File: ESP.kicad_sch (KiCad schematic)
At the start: 23 parts, among them J9 USB_C_Receptacle_USB2.0_16P, U2 TLV1117LV33DCYR, U4 ESP32-C6-MINI-1/U

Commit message: replaced 0805 with 0603, changed logic analyzer symbol and silkscreen
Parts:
- C10, C11, C12, C13, C6, C7, C8, C9: footprint Capacitor_SMD:C_0805_2012Metric -> Capacitor_SMD:C_0603_1608Metric
- D2, D3: footprint LED_SMD:LED_0805_2012Metric -> LED_SMD:LED_0603_1608Metric
- R10, R11, R6, R7, R8, R9: footprint Resistor_SMD:R_0805_2012Metric -> Resistor_SMD:R_0603_1608Metric
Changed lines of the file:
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@@
 			)
 		)
-		(property "Footprint" "Resistor_SMD:R_0805_2012Metric"
+		(property "Footprint" "Resistor_SMD:R_0603_1608Metric"
 			(at 58.166 51.054 90)
 			(effects
@@
 			)
 		)
-		(property "Footprint" "Capacitor_SMD:C_0805_2012Metric"
+		(property "Footprint" "Capacitor_SMD:C_0603_1608Metric"
 			(at 55.5752 151.13 0)
 			(effects
@@
 			)
 		)
-		(property "Footprint" "Capacitor_SMD:C_0805_2012Metric"
+		(property "Footprint" "Capacitor_SMD:C_0603_1608Metric"
 			(at 107.6452 53.34 0)
 			(effects
@@
 			)
 		)
-		(property "Footprint" "Resistor_SMD:R_0805_2012Metric"
+		(property "Footprint" "Resistor_SMD:R_0603_1608Metric"
 			(at 25.146 141.224 90)
 			(effects
@@
 			)
 		)
-		(property "Footprint" "Resistor_SMD:R_0805_2012Metric"
+		(property "Footprint" "Resistor_SMD:R_0603_1608Metric"
 			(at 37.846 141.224 90)
 			(effects
@@
 			)
 		)
-		(property "Footprint" "Resistor_SMD:R_0805_2012Metric"
+		(property "Footprint" "Resistor_SMD:R_0603_1608Metric"
 			(at 94.996 34.544 90)
 			(effects
@@
 			)
 		)
-		(property "Footprint" "Capacitor_SMD:C_0805_2012Metric"
+		(property "Footprint" "Capacitor_SMD:C_0603_1608Metric"
 			(at 49.2252 53.34 0)
 			(effects
@@
 			)
 		)
-		(property "Footprint" "LED_SMD:LED_0805_2012Metric"
+		(property "Footprint" "LED_SMD:LED_0603_1608Metric"
 			(at 36.83 151.13 0)
 			(effects
@@
 			)
 		)
-		(property "Footprint" "Capacitor_SMD:C_0805_2012Metric"
+		(property "Footprint" "Capacitor_SMD:C_0603_1608Metric"
 			(at 35.2552 46.99 0)
 			(effects
@@
 			)
 		)
-		(property "Footprint" "LED_SMD:LED_0805_2012Metric"
+		(property "Footprint" "LED_SMD:LED_0603_1608Metric"
 			(at 24.13 151.13 0)
 			(effects
@@
 			)
 		)
-		(property "Footprint" "Resistor_SMD:R_0805_2012Metric"
+		(property "Footprint" "Resistor_SMD:R_0603_1608Metric"
 			(at 232.791 144.399 90)
 			(effects
@@
 			)
 		)
-		(property "Footprint" "Capacitor_SMD:C_0805_2012Metric"
+		(property "Footprint" "Capacitor_SMD:C_0603_1608Metric"
 			(at 70.8152 92.71 0)
 			(effects
@@
 			)
 		)
-		(property "Footprint" "Capacitor_SMD:C_0805_2012Metric"
+		(property "Footprint" "Capacitor_SMD:C_0603_1608Metric"
 			(at 68.8848 151.13 0)
 			(effects
@@
 			)
 		)
-		(property "Footprint" "Capacitor_SMD:C_0805_2012Metric"
+		(property "Footprint" "Capacitor_SMD:C_0603_1608Metric"
 			(at 216.2302 149.225 0)
 			(effects
@@
 			)
 		)
-		(property "Footprint" "Resistor_SMD:R_0805_2012Metric"
+		(property "Footprint" "Resistor_SMD:R_0603_1608Metric"
 			(at 242.951 144.399 90)
 			(effects
@@
 			)
 		)
-		(property "Footprint" "Capacitor_SMD:C_0805_2012Metric"
+		(property "Footprint" "Capacitor_SMD:C_0603_1608Metric"
 			(at 41.6052 92.71 0)
 			(effects

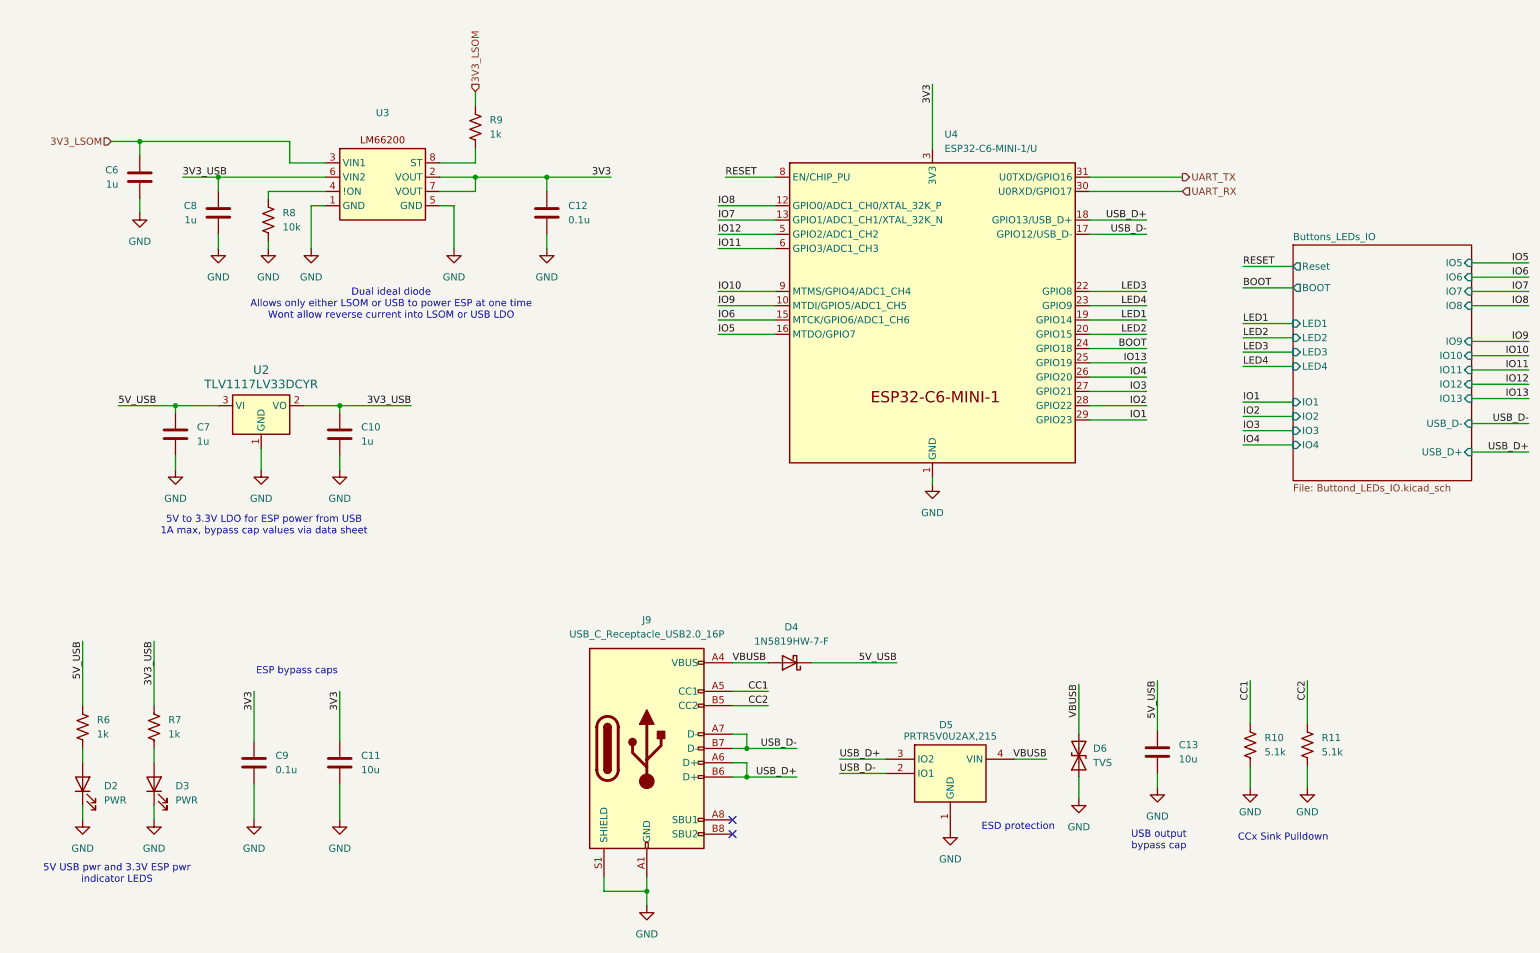
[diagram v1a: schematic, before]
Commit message: changed rpp ic
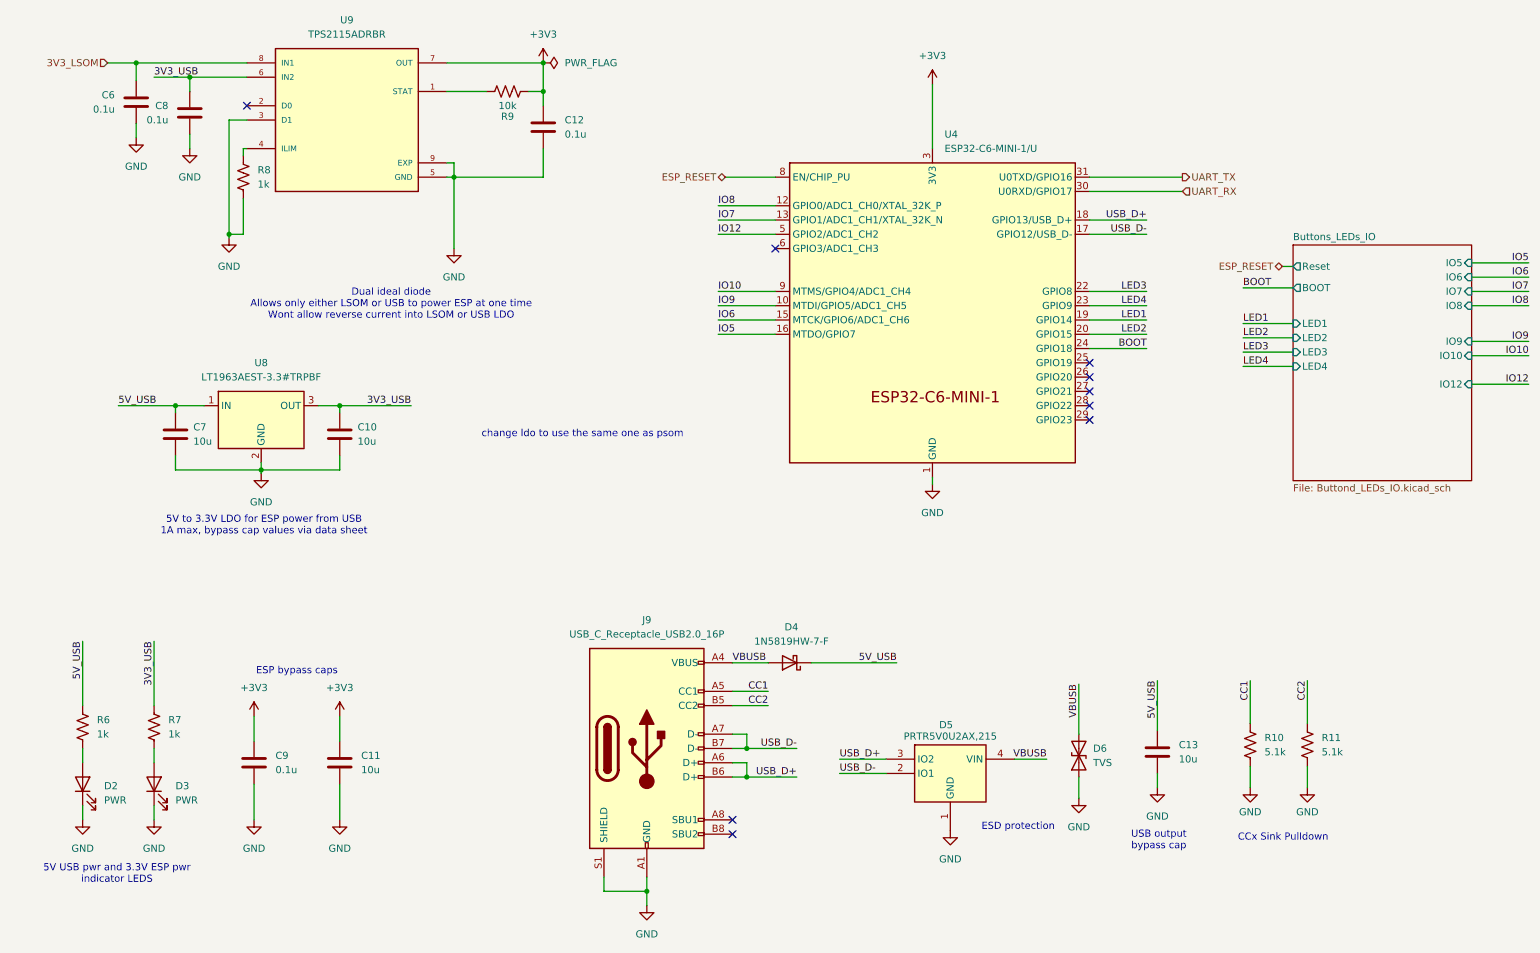
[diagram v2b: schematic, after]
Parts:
- removed U2: TLV1117LV33DCYR, Package_TO_SOT_SMD:SOT-223-3_TabPin2, symbol Regulator_Linear:AMS1117-3.3
- removed U3: ~, UTSVT_Power:SOTFL50P160X60-8N, symbol VCU:LM66200
- added U8: LT1963AEST-3.3#TRPBF, Package_TO_SOT_SMD:SOT-223-3_TabPin2, symbol Regulator_Linear:LT1963AxST-3.3
- added U9: TPS2115ADRBR, Package_SON:VSON-8-1EP_3x3mm_P0.65mm_EP1.65x2.4mm, symbol TPS2115ADRBR:TPS2115ADRBR
- C10, C7: value 1u -> 10u
- C6, C8: value 1u -> 0.1u
- R8: value 10k -> 1k
- R9: value 1k -> 10k
- U4: symbol utsvt_special:ESP32-C6-MINI-1/U -> UTSVT_Special:ESP32-C6-MINI-1/U
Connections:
- net 3V3_LSOM: now also U9.8 (IN1); no longer R9.1
- net 3V3_USB: now also U8.3 (OUT), U9.6 (IN2)
- net 5V_USB: now also U8.1 (IN)
- net GND: now also U8.2 (GND), U9.3 (D1), U9.5 (GND), U9.9 (EXP)
- net at R8.1: now also U9.4 (ILIM)
- net at R9.2: now also U9.1 (STAT)
- net 3V3 renamed +3V3
- net +3V3: now also R9.1, U9.7 (OUT)
- net IO1: no longer names the net of U4.29 (GPIO23)
- net IO11: no longer names the net of U4.6 (GPIO3/ADC1_CH3)
- net IO13: no longer names the net of U4.25 (GPIO19)
- net IO2: no longer names the net of U4.28 (GPIO22)
- net IO3: no longer names the net of U4.27 (GPIO21)
- net IO4: no longer names the net of U4.26 (GPIO20)
- net RESET renamed ESP_RESET
- no-connect marks 2 -> 9
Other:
- sheet Buttons_LEDs_IO ports: added none; removed IO1, IO11, IO13, IO2, IO3, IO4, USB_D+, USB_D-
- note added: "change ldo to use the same one as psom"
- moved on the sheet: C12, C6, C8, R8, R9

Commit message: as;ldfkjasdl;f
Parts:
- removed D5: PRTR5V0U2AX,215, UTSVT_Passives:PRTR5V0U2X, symbol tvs diode:PRTR5V0U2AX,215
- removed U9: TPS2115ADRBR, Package_SON:VSON-8-1EP_3x3mm_P0.65mm_EP1.65x2.4mm, symbol TPS2115ADRBR:TPS2115ADRBR
- added D1: SP0503BAHT, Package_TO_SOT_SMD:SOT-143, symbol UTSVT_ICs:SP0503BAH
- added U1: TPS2115ADRBR, UTSVT_ICs:SON65P300X300X100-9N, symbol UTSVT_ICs:TPS2115ADRBR
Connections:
- net +3V3: now also U1.7 (OUT)
- net 3V3_LSOM: now also U1.8 (IN1)
- net 3V3_USB: now also U1.6 (IN2)
- net GND: now also D1.1 (A), U1.3 (D1), U1.5 (GND), U1.9 (EXP)
- net LED1: now also U4.25 (GPIO19); no longer U4.19 (GPIO14)
- net LED2: now also U4.26 (GPIO20); no longer U4.20 (GPIO15)
- net LED3: now also U4.27 (GPIO21); no longer U4.22 (GPIO8)
- net LED4: now also U4.28 (GPIO22); no longer U4.23 (GPIO9)
- net USB_D+: now also D1.3 (K)
- net USB_D-: now also D1.2 (K)
- net VBUSB: now also D1.4 (K)
- net at R8.1: now also U1.4 (ILIM)
- net at R9.2: now also U1.1 (STAT)

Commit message: maybe final revA revision
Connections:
- net IO10: now also U4.6 (GPIO3/ADC1_CH3); no longer U4.9 (MTMS/GPIO4/ADC1_CH4)
- net IO5: now also U4.15 (MTCK/GPIO6/ADC1_CH6); no longer U4.16 (MTDO/GPIO7)
- net IO6: now also U4.13 (GPIO1/ADC1_CH1/XTAL_32K_N); no longer U4.15 (MTCK/GPIO6/ADC1_CH6)
- net IO7: now also U4.12 (GPIO0/ADC1_CH0/XTAL_32K_P); no longer U4.13 (GPIO1/ADC1_CH1/XTAL_32K_N)
- net IO8: now also U4.10 (MTDI/GPIO5/ADC1_CH5); no longer U4.12 (GPIO0/ADC1_CH0/XTAL_32K_P)
- net IO9: now also U4.9 (MTMS/GPIO4/ADC1_CH4); no longer U4.10 (MTDI/GPIO5/ADC1_CH5)

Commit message: lakshay edits
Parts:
- added 3V31: TestPoint, UTSVT_Special:TestPoint_HEX_3mmID, symbol Connector:TestPoint
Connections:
- net +3V3: now also 3V31.1
- net IO4: now reaches U4.16 (MTDO/GPIO7)
- net LED5: now reaches U4.29 (GPIO23)
- no-connect marks 9 -> 7
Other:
- sheet Buttons_LEDs_IO ports: added IO4, LED5; removed none
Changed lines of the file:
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@@
 	)
 	(junction
+		(at 93.345 22.86)
+		(diameter 0)
+		(color 0 0 0 0)
+	)
+	(junction
 		(at 40.64 83.82)
 		(diameter 0)
@@
 	)
 	(no_connect
-		(at 147.32 71.12)
-	)
-	(no_connect
 		(at 203.2 68.58)
 	)
 	(no_connect
-		(at 203.2 86.36)
-	)
-	(no_connect
 		(at 203.2 71.12)
 	)
@@
 	(wire
 		(pts
-			(xy 88.9 22.86) (xy 106.045 22.86)
+			(xy 93.345 22.86) (xy 106.045 22.86)
+		)
+		(stroke
+			(width 0)
+			(type default)
+		)
+	)
+	(wire
+		(pts
+			(xy 88.9 22.86) (xy 93.345 22.86)
 		)
 		(stroke
@@
 	(wire
 		(pts
+			(xy 230.505 79.375) (xy 239.395 79.375)
+		)
+		(stroke
+			(width 0)
+			(type default)
+		)
+	)
+	(wire
+		(pts
 			(xy 69.85 83.82) (xy 82.55 83.82)
 		)
@@
 	(wire
 		(pts
+			(xy 203.2 86.36) (xy 213.36 86.36)
+		)
+		(stroke
+			(width 0)
+			(type default)
+		)
+	)
+	(wire
+		(pts
 			(xy 69.85 139.065) (xy 69.85 143.51)
 		)
@@
 	(wire
 		(pts
+			(xy 147.32 71.12) (xy 137.16 71.12)
+		)
+		(stroke
+			(width 0)
+			(type default)
+		)
+	)
+	(wire
+		(pts
 			(xy 177.165 132.715) (xy 177.165 140.97)
 		)
@@
 	(wire
 		(pts
+			(xy 271.145 68.58) (xy 281.305 68.58)
+		)
+		(stroke
+			(width 0)
+			(type default)
+		)
+	)
+	(wire
+		(pts
 			(xy 201.295 133.35) (xy 201.295 142.24)
 		)
@@
 		)
 	)
+	(label "IO4"
+		(at 281.305 68.58 180)
+		(effects
+			(font
+				(size 1.27 1.27)
+			)
+			(justify right bottom)
+		)
+	)
 	(label "3V3_USB"
 		(at 36.83 125.73 270)
@@
 		)
 	)
+	(label "LED5"
+		(at 230.505 79.375 0)
+		(effects
+			(font
+				(size 1.27 1.27)
+			)
+			(justify left bottom)
+		)
+	)
 	(label "VBUSB"
 		(at 139.7 129.54 0)
@@
 		)
 	)
+	(label "IO4"
+		(at 137.16 71.12 0)
+		(effects
+			(font
+				(size 1.27 1.27)
+			)
+			(justify left bottom)
+		)
+	)
 	(label "LED3"
 		(at 213.36 81.28 180)
@@
 		)
 	)
+	(label "LED5"
+		(at 213.36 86.36 180)
+		(effects
+			(font
+				(size 1.27 1.27)
+			)
+			(justify right bottom)
+		)
+	)
 	(label "5V_USB"
 		(at 215.265 132.715 270)
@@
 	)
 	(symbol
+		(lib_id "Connector:TestPoint")
+		(at 93.345 22.86 0)
+		(unit 1)
+		(exclude_from_sim no)
+		(in_bom yes)
+		(on_board yes)
+		(dnp no)
+		(property "Reference" "3V31"
+			(at 92.329 14.986 0)
+			(effects
+				(font
+					(size 1.27 1.27)
+				)
+				(justify left)
+			)
+		)
+		(property "Value" "TestPoint"
+			(at 92.329 17.272 0)
+			(effects
+				(font
+					(size 1.27 1.27)
+				)
+				(justify left)
+			)
+		)
+		(property "Footprint" "UTSVT_Special:TestPoint_HEX_3mmID"
+			(at 98.425 22.86 0)
+			(effects
+				(font
+					(size 1.27 1.27)
+				)
+				(hide yes)
+			)
+		)
+		(property "Datasheet" "~"
+			(at 98.425 22.86 0)
+			(effects
+				(font
+					(size 1.27 1.27)
+				)
+				(hide yes)
+			)
+		)
+		(property "Description" "test point"
+			(at 93.345 22.86 0)
+			(effects
+				(font
+					(size 1.27 1.27)
+				)
+				(hide yes)
+			)
+		)
+		(pin "1"
+		)
+		(instances
+			(project "VehicleControlUnit"
+				(path "/795c8e51-3ded-4d21-b864-aaff31c5def7/6282503b-e4ab-454b-a074-f701a067f39b"
+					(reference "3V31")
+					(unit 1)
+				)
+			)
+		)
+	)
+	(symbol
 		(lib_id "Device:R_US")
 		(at 231.775 144.145 0)
@@
 			(effects
 				(font
+					(size 1.27 1.27)
+				)
+				(justify right)
+			)
+		)
+		(pin "LED5" input
+			(at 239.395 79.375 180)
+			(effects
+				(font
+					(size 1.27 1.27)
+				)
+				(justify left)
+			)
+		)
+		(pin "IO4" input
+			(at 271.145 68.58 0)
+			(effects
+				(font

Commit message: ravi's bs
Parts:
- removed D6: TVS, Diode_SMD:D_0603_1608Metric, symbol Device:D_TVS
- R6: value 1k -> 450
- R7: value 1k -> 120
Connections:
- net UART_RX: now also U4.31 (U0TXD/GPIO16); no longer U4.30 (U0RXD/GPIO17)
- net UART_TX: now also U4.30 (U0RXD/GPIO17); no longer U4.31 (U0TXD/GPIO16)
- net LED5: no longer names the net of U4.29 (GPIO23)
- no-connect marks 7 -> 8
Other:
- sheet Buttons_LEDs_IO ports: added none; removed LED5
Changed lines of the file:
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@@
 	)
 	(no_connect
+		(at 203.2 86.36)
+	)
+	(no_connect
 		(at 203.2 68.58)
 	)
@@
 	(wire
 		(pts
-			(xy 230.505 79.375) (xy 239.395 79.375)
-		)
-		(stroke
-			(width 0)
-			(type default)
-		)
-	)
-	(wire
-		(pts
 			(xy 69.85 83.82) (xy 82.55 83.82)
 		)
@@
 	(wire
 		(pts
-			(xy 203.2 86.36) (xy 213.36 86.36)
-		)
-		(stroke
-			(width 0)
-			(type default)
-		)
-	)
-	(wire
-		(pts
 			(xy 69.85 139.065) (xy 69.85 143.51)
 		)
@@
 	(wire
 		(pts
-			(xy 201.295 149.86) (xy 201.295 153.67)
-		)
-		(stroke
-			(width 0)
-			(type default)
-		)
-	)
-	(wire
-		(pts
 			(xy 175.26 96.52) (xy 175.26 97.79)
 		)
@@
 	(wire
 		(pts
-			(xy 201.295 133.35) (xy 201.295 142.24)
-		)
-		(stroke
-			(width 0)
-			(type default)
-		)
-	)
-	(wire
-		(pts
 			(xy 88.9 40.64) (xy 90.17 40.64)
 		)
@@
 		)
 	)
-	(label "VBUSB"
-		(at 201.295 133.35 270)
-		(effects
-			(font
-				(size 1.27 1.27)
-			)
-			(justify right bottom)
-		)
-	)
 	(label "IO9"
 		(at 137.16 63.5 0)
@@
 		)
 	)
-	(label "LED5"
-		(at 230.505 79.375 0)
-		(effects
-			(font
-				(size 1.27 1.27)
-			)
-			(justify left bottom)
-		)
-	)
 	(label "VBUSB"
 		(at 139.7 129.54 0)
@@
 		)
 	)
-	(label "LED5"
-		(at 213.36 86.36 180)
-		(effects
-			(font
-				(size 1.27 1.27)
-			)
-			(justify right bottom)
-		)
-	)
 	(label "5V_USB"
 		(at 215.265 132.715 270)
@@
 	(hierarchical_label "UART_TX"
 		(shape output)
-		(at 219.71 43.18 0)
+		(at 219.71 45.72 0)
 		(effects
 			(font
@@
 	(hierarchical_label "UART_RX"
 		(shape input)
-		(at 219.71 45.72 0)
+		(at 219.71 43.18 0)
 		(effects
 			(font
@@
 			)
 		)
-		(property "Value" "1k"
+		(property "Value" "450"
 			(at 26.67 142.2399 0)
 			(effects
@@
 			)
 		)
-		(property "Value" "1k"
+		(property "Value" "120"
 			(at 39.37 142.2399 0)
 			(effects
@@
 	(symbol
 		(lib_id "power:GND")
-		(at 201.295 153.67 0)
-		(unit 1)
-		(exclude_from_sim no)
-		(in_bom yes)
-		(on_board yes)
-		(dnp no)
-		(fields_autoplaced yes)
-		(property "Reference" "#PWR049"
-			(at 201.295 160.02 0)
-			(effects
-				(font
-					(size 1.27 1.27)
-				)
-				(hide yes)
-			)
-		)
-		(property "Value" "GND"
-			(at 201.295 158.75 0)
-			(effects
-				(font
-					(size 1.27 1.27)
-				)
-			)
-		)
-		(property "Footprint" ""
-			(at 201.295 153.67 0)
-			(effects
-				(font
-					(size 1.27 1.27)
-				)
-				(hide yes)
-			)
-		)
-		(property "Datasheet" ""
-			(at 201.295 153.67 0)
-			(effects
-				(font
-					(size 1.27 1.27)
-				)
-				(hide yes)
-			)
-		)
-		(property "Description" "Power symbol creates a global label with name \"GND\" , ground"
-			(at 201.295 153.67 0)
-			(effects
-				(font
-					(size 1.27 1.27)
-				)
-				(hide yes)
-			)
-		)
-		(pin "1"
-		)
-		(instances
-			(project "VehicleControlUnit"
-				(path "/795c8e51-3ded-4d21-b864-aaff31c5def7/6282503b-e4ab-454b-a074-f701a067f39b"
-					(reference "#PWR049")
-					(unit 1)
-				)
-			)
-		)
-	)
-	(symbol
-		(lib_id "power:GND")
 		(at 69.85 157.48 0)
 		(unit 1)
@@
 	)
 	(symbol
-		(lib_id "Device:D_TVS")
-		(at 201.295 146.05 90)
-		(unit 1)
-		(exclude_from_sim no)
-		(in_bom yes)
-		(on_board yes)
-		(dnp no)
-		(fields_autoplaced yes)
-		(property "Reference" "D6"
-			(at 203.835 144.7799 90)
-			(effects
-				(font
-					(size 1.27 1.27)
-				)
-				(justify right)
-			)
-		)
-		(property "Value" "TVS"
-			(at 203.835 147.3199 90)
-			(effects
-				(font
-					(size 1.27 1.27)
-				)
-				(justify right)
-			)
-		)
-		(property "Footprint" "Diode_SMD:D_0603_1608Metric"
-			(at 201.295 146.05 0)
-			(effects
-				(font
-					(size 1.27 1.27)
-				)
-				(hide yes)
-			)
-		)
-		(property "Datasheet" "~"
-			(at 201.295 146.05 0)
-			(effects
-				(font
-					(size 1.27 1.27)
-				)
-				(hide yes)
-			)
-		)
-		(property "Description" "Bidirectional transient-voltage-suppression diode"
-			(at 201.295 146.05 0)
-			(effects
-				(font
-					(size 1.27 1.27)
-				)
-				(hide yes)
-			)
-		)
-		(property "P/N" "CPDUC5V0R-HF "
-			(at 201.295 146.05 0)
-			(effects
-				(font
-					(size 1.27 1.27)
-				)
-				(hide yes)
-			)
-		)
-		(pin "1"
-		)
-		(pin "2"
-		)
-		(instances
-			(project "VehicleControlUnit"
-				(path "/795c8e51-3ded-4d21-b864-aaff31c5def7/6282503b-e4ab-454b-a074-f701a067f39b"
-					(reference "D6")
-					(unit 1)
-				)
-			)
-		)
-	)
-	(symbol
 		(lib_id "power:+3V3")
 		(at 175.26 26.67 0)
@@
 			)
 		)
-		(pin "LED5" input
-			(at 239.395 79.375 180)
-			(effects
-				(font
-					(size 1.27 1.27)
-				)
-				(justify left)
-			)
-		)

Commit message: more bom stuff
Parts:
- C10, C11, C13, C7: footprint Capacitor_SMD:C_0603_1608Metric -> Capacitor_SMD:C_0805_2012Metric
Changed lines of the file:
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@@
 			)
 		)
-		(property "Footprint" "Capacitor_SMD:C_0603_1608Metric"
+		(property "Footprint" "Capacitor_SMD:C_0805_2012Metric"
 			(at 70.8152 92.71 0)
 			(effects
@@
 			)
 		)
-		(property "Footprint" "Capacitor_SMD:C_0603_1608Metric"
+		(property "Footprint" "Capacitor_SMD:C_0805_2012Metric"
 			(at 68.8848 151.13 0)
 			(effects
@@
 			)
 		)
-		(property "Footprint" "Capacitor_SMD:C_0603_1608Metric"
+		(property "Footprint" "Capacitor_SMD:C_0805_2012Metric"
 			(at 216.2302 149.225 0)
 			(effects
@@
 			)
 		)
-		(property "Footprint" "Capacitor_SMD:C_0603_1608Metric"
+		(property "Footprint" "Capacitor_SMD:C_0805_2012Metric"
 			(at 41.6052 92.71 0)
 			(effects
